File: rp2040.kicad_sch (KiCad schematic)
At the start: 25 parts, among them J13 Conn_01x02, J14 Conn_01x06, U6 RP2040, U7 W25Q32JVSS, Y1 12.0MHz

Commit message: the great renaming
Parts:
- renumbered C14 to C12, C15 to C13, C16 to C14, C17 to C15, C18 to C16, C19 to C17, C20 to C18, C21 to C19, C22 to C20, C23 to C21, C24 to C22, C25 to C23, C26 to C24, J13 to J10, J14 to J11, R11 to R10, R12 to R11, R13 to R12, R14 to R13, R15 to R14, R16 to R15, R10 to R9, U6 to U4, U7 to U5

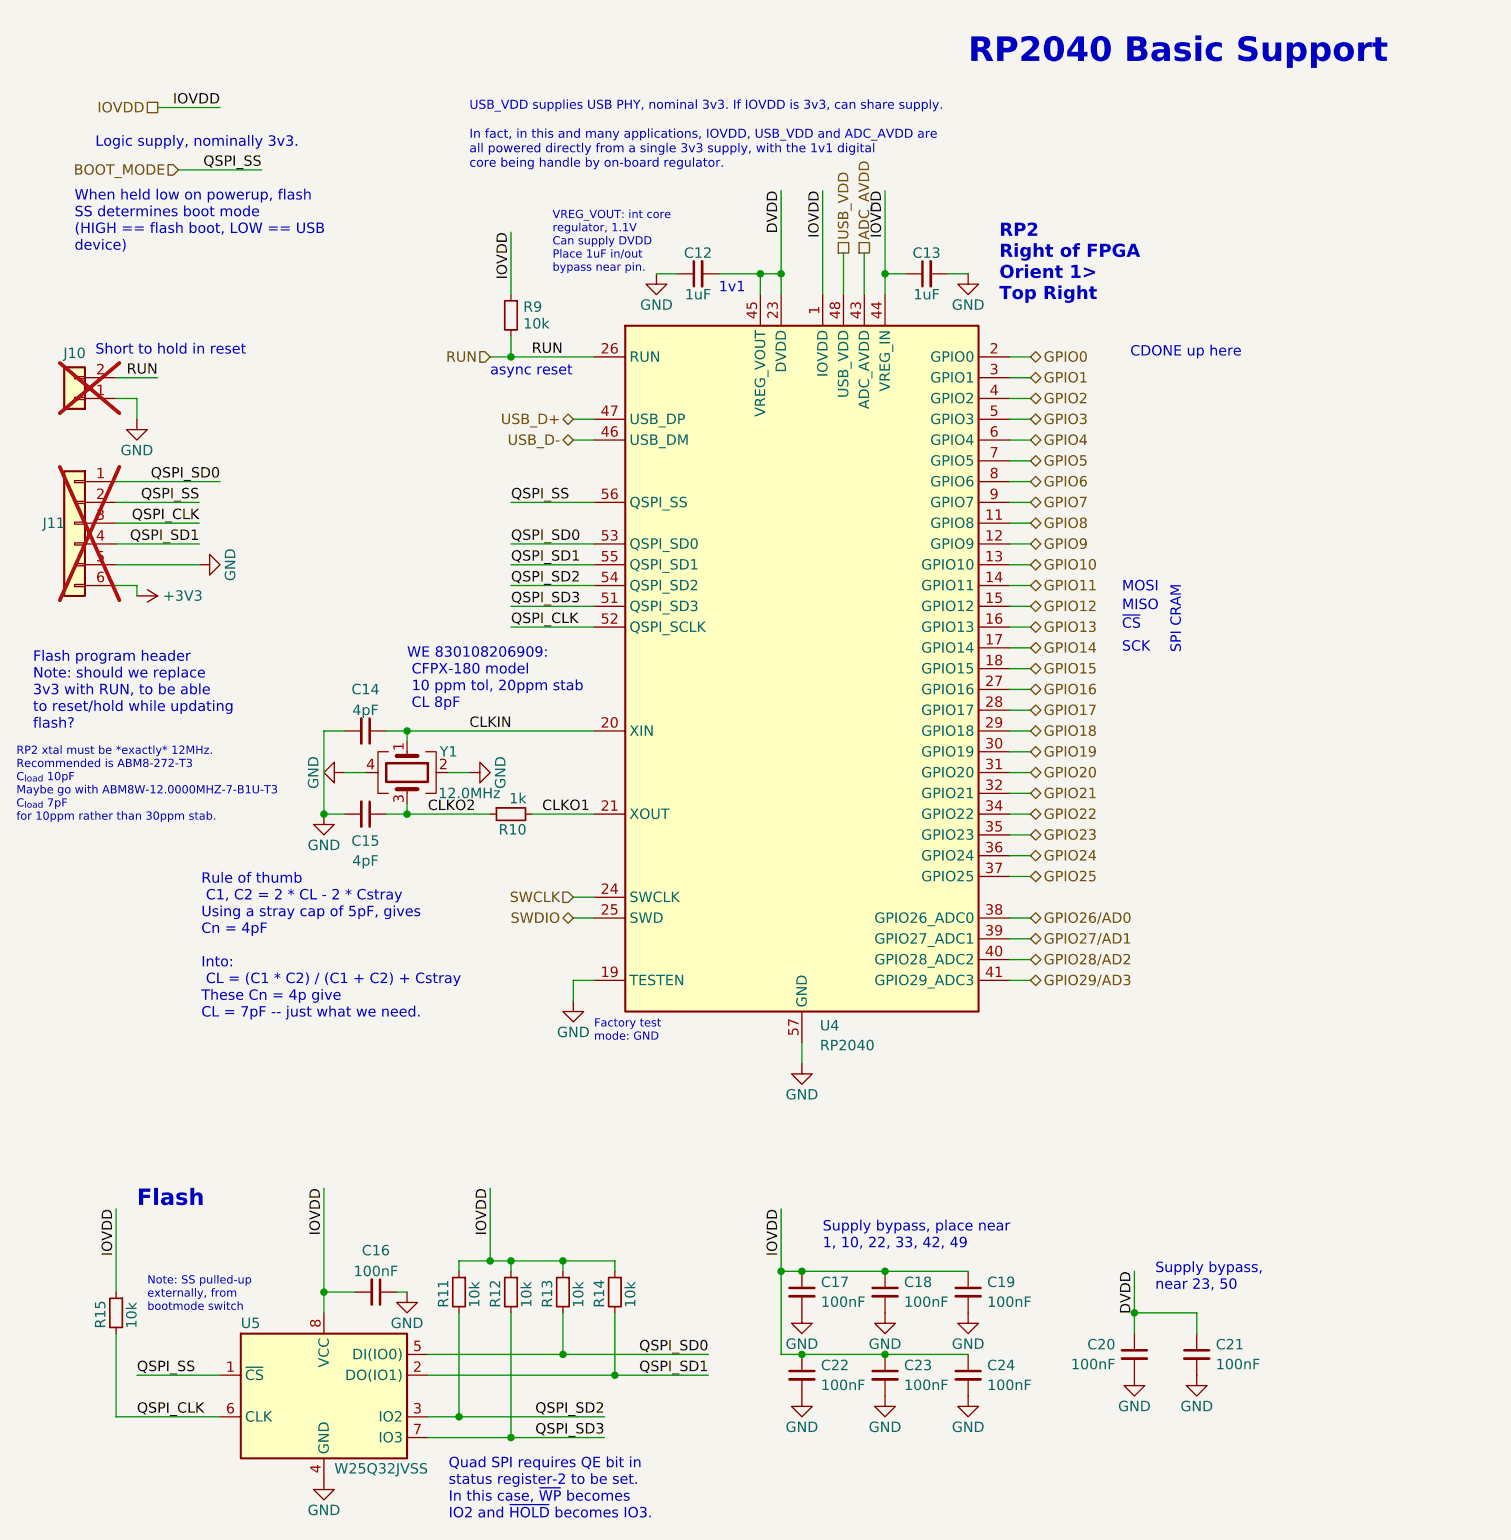
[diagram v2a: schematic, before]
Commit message: logo rework, relabelling, for efab run
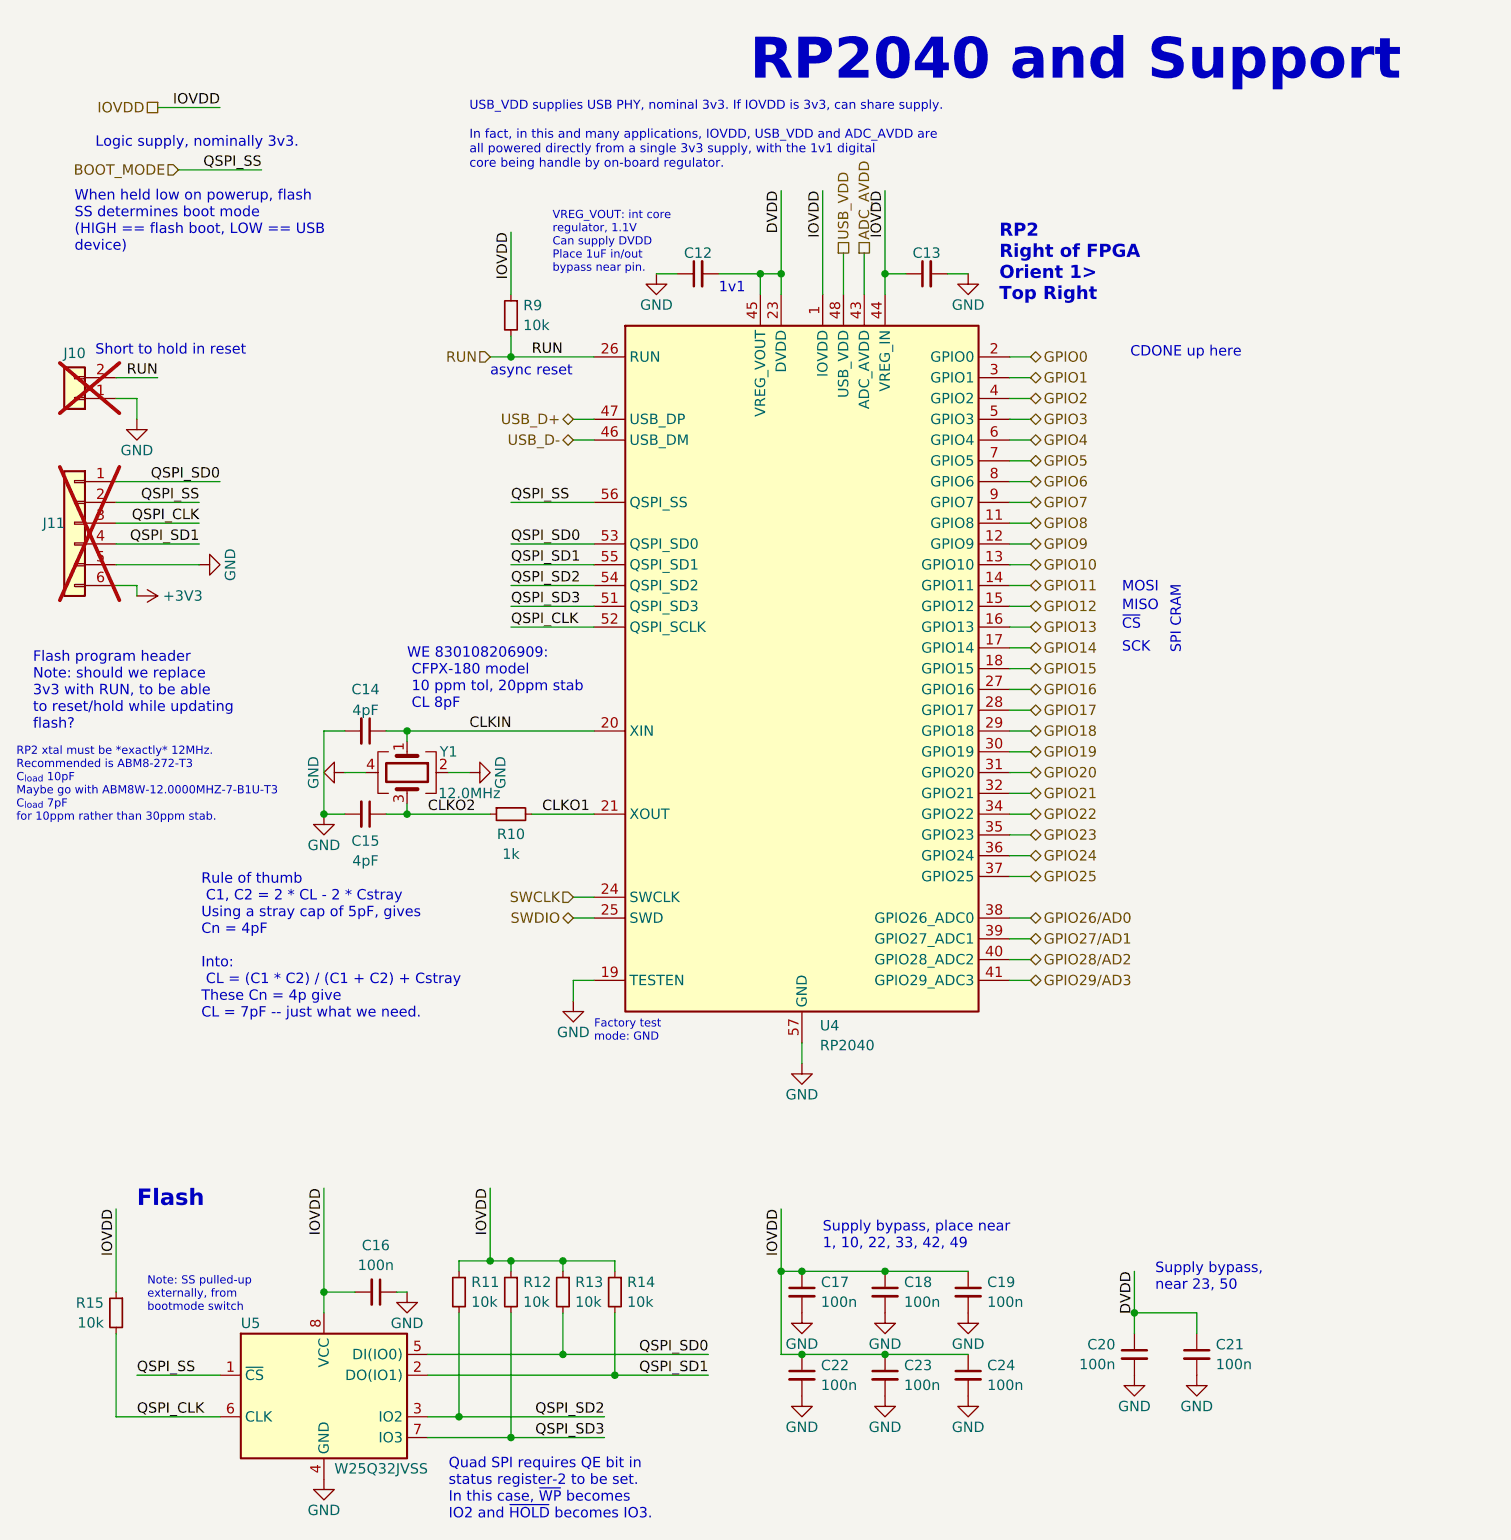
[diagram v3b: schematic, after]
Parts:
- C12, C13: value 1uF -> C_1u_0603_50V; DigikeyPN (none) -> 490-12330-1-ND; Display Value (none) -> 1u; Display_Value (none) -> 1u
- C14, C15: DigikeyPN (none) -> 311-3643-1-ND
- C16, C17, C18, C19, C20, C21, C22, C23, C24: value 100nF -> C_100n_0402_50V; DigikeyPN (none) -> 490-13342-1-ND; Display Value (none) -> 100n; Display_Value (none) -> 100n; MPN CL05A104KA5NNNC -> GRM155R71H104KE14J
- R10: value 1k -> R_1k_0402; DigikeyPN (none) -> CR0402-FX-1001GLFCT-ND; Display Value (none) -> 1k; Display_Value (none) -> 1k
- R11, R12, R13, R14, R15, R9: value 10k -> R_10k_0402; DigikeyPN (none) -> 10-ERJ-U02F1002XCT-ND; Display Value (none) -> 10k; Display_Value (none) -> 10k
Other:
- note added: "RP2040 and Support"
- note removed: "RP2040 Basic Support"

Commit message: revision bump
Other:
- company: Psychogenic Technologies  -> Psychogenic Technologies for efabless
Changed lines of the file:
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@@
 	(title_block
 		(title "Tiny Tapeout 4/5 Demo Board")
-		(date "2024-12-26")
-		(rev "1.0")
-		(company "Psychogenic Technologies ")
-		(comment 1 "(C) 2024 Pat Deegan")
+		(date "2025-02-21")
+		(rev "1.2")
+		(company "Psychogenic Technologies for efabless")
+		(comment 1 "(C) 2024-2025 Pat Deegan")
 	)
 	(text "CDONE up here"
@@
 			"kQMAAAAAAACwZJdi01UAAOCcTda/fwAAIAAAAAAAAABwAwAAAAAAAFh/Xdi/fwAAAQAAAAAAAAAA"
 			"AAAAAAAAAAAAAAAAAAAA6JX2f79/AADvza20n+tI/bCLwR0FJ+8hMAAAAAAAAABQVpdi01UAAABM"
-			"U0XOAwAAAAAAAAAAAAAAdC5jAAAAAAAAAA=="
+			"U0XOAwAAAAAAAAAAAAAAdC5jAAAAAAAAAABxAAAAagAAAGUAAAArAAAAOQAAADEAAABXAAAAbwAA"
+			"AEMAAAB3AAAATgAAAE4AAABRAAAAcAAAAEEAAABRAAAANwAAAG4AAABRAAAAdAAAAEUAAABNAAAA"
+			"dQAAADgAAABHAAAAYgAAAFYAAABsAAAATgAAAEMAAABRAAAAVwAAAG8AAABqAAAAcAAAAE8AAAAr"
+			"AAAAWQAAAFYAAABDAAAAWgAAAGYAAAB5AAAAVQAAAFEAAABBAAAAQQAAAGUAAABVAAAANQAAAFMA"
+			"AABZAAAAdgAAADAAAABnAAAAUgAAADYAAABOAAAAbQAAAGwAAABWAAAATwAAAHAAAABpAAAARwAA"
+			"ADgAAAB6AAAAUgAAAEsAAABsAAAAbAAAAFQAAAA4AAAAegAAAGEAAABtAAAAZgAAAHcAAAByAAAA"
+			"RwAAADkAAABhAAAAZAAAAEUAAABlAAAAUAAAAHQAAABlAAAAawAAAFUAAABpAAAAawAAAFMAAABo"
+			"AAAAMgAAAHMAAABYAAAAKwAAAGcAAAA2AAAAcQAAAHIAAABTAAAAawAAADkAAABVAAAAZgAAAHEA"
+			"AABHAAAANAAAAEEAAABUAAAATQAAAHYAAABKAAAAYQAAADMAAAA2AAAATAAAAEQAAAA1AAAAMgAA"
+			"AGcAAABiAAAATAAAADMAAABIAAAAcwAAAHYAAAB0AAAAWAAAADcAAABKAAAAbgAAAGYAAABZAAAA"
+			"MQAAAGQAAAArAAAATwAAAHQAAAAzAAAAVAAAAHoAAABwAAAAaQAAAFEAAAB5AAAAWAAAAFQAAABU"
+			"AAAAcAAAAEIAAAA1AAAAdAAAAGwAAABtAAAARAAAADYAAABYAAAASwAAADYAAABoAAAAUAAAAHQA"
+			"AABkAAAAKwAAAHgAAAB0AAAAYwAAAC8AAAB6AAAASAAAAFoAAAA0AAAALwAAAFkAAABvAAAARwAA"
+			"ADAAAAAzAAAAaQAAADQAAAA3AAAAMQAAAGoAAAByAAAAaQAAAGgAAABmAAAASwAAAFoAAABRAAAA"
+			"RAAAADAAAABSAAAAcwAAADIAAABOAAAARQAAAG8AAABZAAAARQAAADIAAABCAAAAdAAAADEAAABi"
+			"AAAAbgAAAGYAAABhAAAAZAAAAEMAAAB1AAAANQAAADAAAABHAAAAMwAAAEIAAAB2AAAANQAAAHcA"
+			"AABIAAAANgAAAGgAAAB2AAAAYgAAAEIAAABTAAAAeAAAAGUAAABOAAAASgAAAHIAAABiAAAAbwAA"
+			"AGkAAABvAAAAUwAAAFgAAABzAAAAYQAAAHYAAABuAAAAcgAAADEAAABrAAAANwAAAGIAAABjAAAA"
+			"cgAAAEYAAAA4AAAAMwAAADUAAABkAAAATQ=="
 		)
 	)
